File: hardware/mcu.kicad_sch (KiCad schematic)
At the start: 19 parts, among them J2 BOOT, J3 Conn_01x04_Male, U1 STM32F103C8Tx, Y1 8MHz, Y2 32KHz

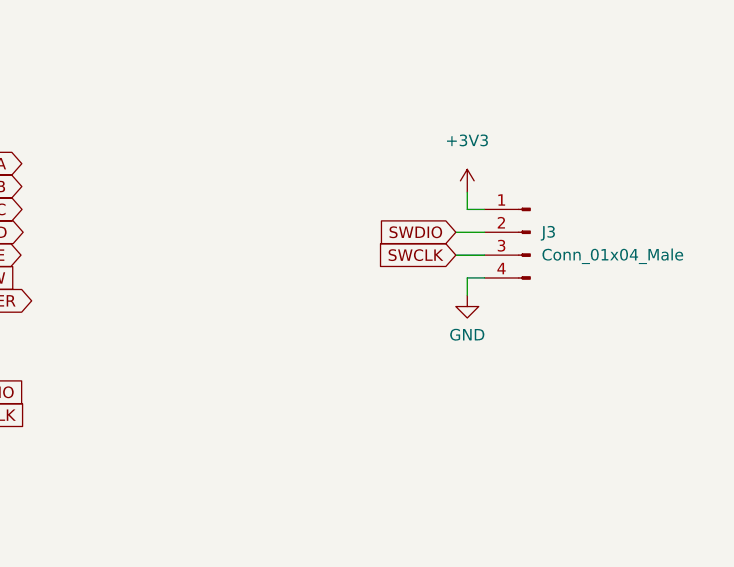
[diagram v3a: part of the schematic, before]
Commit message: Footprints are assigned and Cut edges fixed
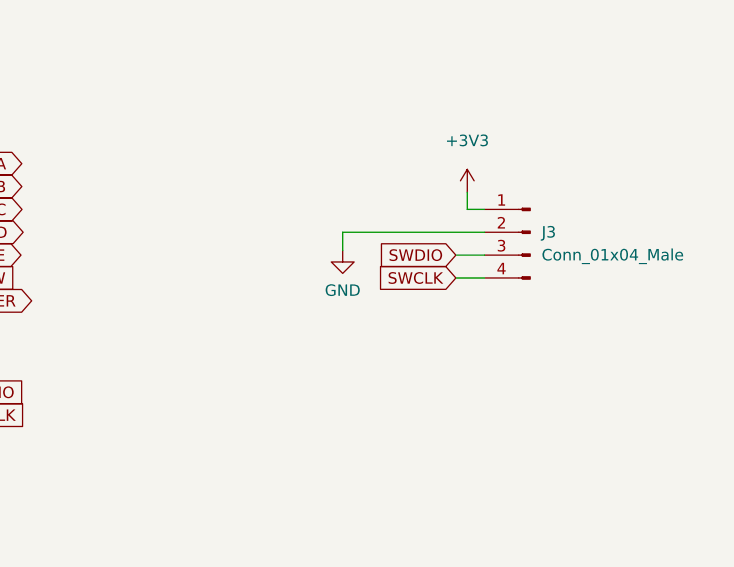
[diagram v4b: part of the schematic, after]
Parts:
- C11, C4, C6: footprint Capacitor_SMD:CP_Elec_6.3x7.7 -> Capacitor_SMD:C_0603_1608Metric
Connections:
- net GND: now also J3.2 (Pin_2); no longer J3.4 (Pin_4)
- net SWCLK: now also J3.4 (Pin_4); no longer J3.3 (Pin_3)
- net SWDIO: now also J3.3 (Pin_3); no longer J3.2 (Pin_2)
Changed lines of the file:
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@@
     (stroke (width 0) (type default) (color 0 0 0 0))
   )
-  (wire (pts (xy 227.965 104.14) (xy 231.14 104.14))
+  (wire (pts (xy 227.965 106.68) (xy 231.14 106.68))
     (stroke (width 0) (type default) (color 0 0 0 0))
   )
@@
     (stroke (width 0) (type default) (color 0 0 0 0))
   )
+  (wire (pts (xy 231.14 104.14) (xy 215.392 104.14))
+    (stroke (width 0) (type default) (color 0 0 0 0))
+  )
   (wire (pts (xy 210.82 34.29) (xy 210.82 35.56))
     (stroke (width 0) (type default) (color 0 0 0 0))
@@
     (stroke (width 0) (type default) (color 0 0 0 0))
   )
-  (wire (pts (xy 229.235 111.125) (xy 229.235 109.22))
+  (wire (pts (xy 215.392 104.14) (xy 215.392 106.172))
     (stroke (width 0) (type default) (color 0 0 0 0))
   )
@@
     (stroke (width 0) (type default) (color 0 0 0 0))
   )
-  (wire (pts (xy 227.965 106.68) (xy 231.14 106.68))
+  (wire (pts (xy 227.965 109.22) (xy 231.14 109.22))
     (stroke (width 0) (type default) (color 0 0 0 0))
   )
   (wire (pts (xy 34.925 109.855) (xy 33.655 109.855))
-    (stroke (width 0) (type default) (color 0 0 0 0))
-  )
-  (wire (pts (xy 229.235 109.22) (xy 231.14 109.22))
     (stroke (width 0) (type default) (color 0 0 0 0))
   )
@@
     )
   )
-  (global_label "SWDIO" (shape input) (at 227.965 104.14 180) (fields_autoplaced)
-    (effects (font (size 1.27 1.27)) (justify right))
-    (property "Intersheet References" "${INTERSHEET_REFS}" (id 0) (at 219.6857 104.2194 0)
+  (global_label "SWDIO" (shape input) (at 227.965 106.68 180) (fields_autoplaced)
+    (effects (font (size 1.27 1.27)) (justify right))
+    (property "Intersheet References" "${INTERSHEET_REFS}" (id 0) (at 219.6857 106.7594 0)
       (effects (font (size 1.27 1.27)) (justify right) hide)
     )
@@
     )
   )
-  (global_label "SWCLK" (shape input) (at 227.965 106.68 180) (fields_autoplaced)
-    (effects (font (size 1.27 1.27)) (justify right))
-    (property "Intersheet References" "${INTERSHEET_REFS}" (id 0) (at 219.3229 106.7594 0)
+  (global_label "SWCLK" (shape input) (at 227.965 109.22 180) (fields_autoplaced)
+    (effects (font (size 1.27 1.27)) (justify right))
+    (property "Intersheet References" "${INTERSHEET_REFS}" (id 0) (at 219.3229 109.2994 0)
       (effects (font (size 1.27 1.27)) (justify right) hide)
     )
@@
     )
   )
-  (symbol (lib_id "power:GND") (at 229.235 111.125 0) (unit 1)
-    (in_bom yes) (on_board yes) (fields_autoplaced)
-    (property "Reference" "#PWR015" (id 0) (at 229.235 117.475 0)
-      (effects (font (size 1.27 1.27)) hide)
-    )
-    (property "Value" "GND" (id 1) (at 229.235 115.57 0))
-    (property "Footprint" "" (id 2) (at 229.235 111.125 0)
-      (effects (font (size 1.27 1.27)) hide)
-    )
-    (property "Datasheet" "" (id 3) (at 229.235 111.125 0)
+  (symbol (lib_id "power:GND") (at 215.392 106.172 0) (unit 1)
+    (in_bom yes) (on_board yes) (fields_autoplaced)
+    (property "Reference" "#PWR015" (id 0) (at 215.392 112.522 0)
+      (effects (font (size 1.27 1.27)) hide)
+    )
+    (property "Value" "GND" (id 1) (at 215.392 110.617 0))
+    (property "Footprint" "" (id 2) (at 215.392 106.172 0)
+      (effects (font (size 1.27 1.27)) hide)
+    )
+    (property "Datasheet" "" (id 3) (at 215.392 106.172 0)
       (effects (font (size 1.27 1.27)) hide)
     )
@@
       (effects (font (size 1.27 1.27)) (justify left))
     )
-    (property "Footprint" "Capacitor_SMD:CP_Elec_6.3x7.7" (id 2) (at 148.59 49.53 0)
+    (property "Footprint" "Capacitor_SMD:C_0603_1608Metric" (id 2) (at 148.59 49.53 0)
       (effects (font (size 1.27 1.27)) hide)
     )
@@
       (effects (font (size 1.27 1.27)) (justify left))
     )
-    (property "Footprint" "Capacitor_SMD:CP_Elec_6.3x7.7" (id 2) (at 192.405 33.655 0)
+    (property "Footprint" "Capacitor_SMD:C_0603_1608Metric" (id 2) (at 192.405 33.655 0)
       (effects (font (size 1.27 1.27)) hide)
     )
@@
       (effects (font (size 1.27 1.27)) (justify left))
     )
-    (property "Footprint" "Capacitor_SMD:CP_Elec_6.3x7.7" (id 2) (at 233.045 60.325 0)
-      (effects (font (size 1.27 1.27)) hide)
-    )
+    (property "Footprint" "Capacitor_SMD:C_0603_1608Metric" (id 2) (at 233.045 60.325 0)
+      (effects (font (size 1.27 1.27)) hide)
+    )

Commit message: yeni seyler eklendi
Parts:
- removed C1, C2: 20pF, Capacitor_SMD:C_0603_1608Metric, symbol Device:C_Small
- removed C10, C5, C7, C8, C9: 100nF, Capacitor_SMD:C_0603_1608Metric, symbol Device:C_Small
- removed C11, C6: 1uF/6V, Capacitor_SMD:C_0603_1608Metric, symbol Device:C_Polarized_Small
- removed C4: 1uF/10V, Capacitor_SMD:C_0603_1608Metric, symbol Device:C_Polarized_Small
- removed R3: 100R, Resistor_SMD:R_0603_1608Metric, symbol Device:R_Small
- removed U1: STM32F103C8Tx, Package_QFP:LQFP-48_7x7mm_P0.5mm, symbol MCU_ST_STM32F1:STM32F103C8Tx
- removed Y1: 8MHz, Crystal:Crystal_SMD_HC49-SD, symbol Device:Crystal_Small
- removed Y2: 32KHz, Crystal:Crystal_C38-LF_D3.0mm_L8.0mm_Vertical, symbol Device:Crystal_Small
- added U?: STM32G030F6P6TR, TSSOP20, symbol STM32G030F6P6TR:STM32G030F6P6TR
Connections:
- net BTN_IO: now also U?.1 (PB7/PB8)
- net BTN_MODE: now also U?.15 (PB0/PB1/PB2/PA8)
- net BTN_START: now also U?.20 (PB3/PB4/PB5/PB6)
- net BUZZER: now also U?.16 (PA11)
- net DISP_A: now also U?.11 (PA4)
- net DISP_B: now also U?.10 (PA3)
- net DISP_C: now also U?.9 (PA2)
- net DISP_D: now also U?.8 (PA1)
- net DISP_E: now also U?.7 (PA0)
- net DISP_F: now also U?.12 (PA5)
- net DISP_G: now also U?.13 (PA6)
- net DISP_P: now also U?.14 (PA7)
- net FLOW: now also U?.17 (PA12)
- net GND: now also U?.5 (VSS/VSSA)
- net RELAY: now also U?.2 (PB9/PC14-OSC32_IN)
- net SWCLK: now also U?.18 (PA13)
- net SWDIO: now also U?.19 (PA15/PA14-BOOT0)
- new net NRST: U?.6 (NRST)
- no-connect marks 17 -> 0
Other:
- note added: "Buzzer"
- note added: "Connectors"
- note added: "MCU"
- note removed: "Crystal Oscillators"
- moved on the sheet: J3
